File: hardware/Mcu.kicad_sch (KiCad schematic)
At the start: 9 parts, among them U10 STM32G484VEHx, Y1 X322516MLB4SI

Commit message: inductors 3d models fix, smaller relay (same series as the one from IMD), other + sync
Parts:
- added C70: 22uF, Capacitor_SMD:C_0805_2012Metric, symbol Device:C_Small
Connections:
- net +3.3V: now also C70.1
- net GND: now also C70.2
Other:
- moved on the sheet: C23, C24, C25, C28, C29

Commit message: all but the communications sections done
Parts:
- added R3: 0, Resistor_SMD:R_0603_1608Metric, symbol Device:R_Small
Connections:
- net +3.3V: now also R3.1; no longer C23.1, C24.1, C25.1, C28.1, C29.1, C70.1, U10.D5 (VDD), U10.D7 (VDD), U10.F5 (VDD), U10.F7 (VDD), U10.J5 (VDDA), U10.K5 (VREF+)
- new net +3.3VIO: C23.1, C24.1, C25.1, C28.1, C29.1, C70.1, R3.2, U10.D5 (VDD), U10.D7 (VDD), U10.F5 (VDD), U10.F7 (VDD), U10.J5 (VDDA), U10.K5 (VREF+)

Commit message: sync
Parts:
- added C36: 22uF, Capacitor_SMD:C_0805_2012Metric, symbol Device:C_Small
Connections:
- net +3.3VIO: now also C36.1
- net EN_12V: now also U10.F2 (PC0)
- net GND: now also C36.2
- net PG_12V: now also U10.F4 (PC1)
- net LTC_MISO renamed COM_MISO
- net LTC_MOSI renamed COM_MOSI
- net LTC_SCK renamed COM_SCK
- net SENS_IMD: no longer names the net of U10.J4 (PB2)
- net ~{LTC_CS} renamed ~{COM_CS}
- no-connect marks 38 -> 37
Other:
- note removed: "TIM5_CH1"
- moved on the sheet: C23, C24, C25, C28, C29, C70, R3

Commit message: sync
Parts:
- C23, C24, C25, C28, C29: Mouser Price/Stock (none) -> https://www.mouser.pl/ProductDetail/KEMET/C0603C104J3RACTU?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
- C36, C70: Mouser Price/Stock (none) -> https://www.mouser.pl/ProductDetail/Samsung-Electro-Mechani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
- U10: Mouser Part Number (none) -> 511-STM32G484VEH6; Mouser Price/Stock (none) -> https://www.mouser.pl/ProductDetail/STMicroelectronics/STM3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
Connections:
- net SPI_RDY: now reaches U10.F1 (PC2)
- net ~{FLT}: now reaches U10.G1 (PC3)
- no-connect marks 37 -> 35
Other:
- moved on the sheet: C36, C70, R3

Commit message: some routing done
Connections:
- net PG_12V: now also U10.G2 (PA1); no longer U10.F4 (PC1)
- net SIGNAL_AMS_ERROR: now also U10.J8 (PB10); no longer U10.H7 (PE15)
- net SIGNAL_LED_2: now also U10.H1 (PA2); no longer U10.H6 (PE9)
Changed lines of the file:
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@@
 	)
 	(no_connect
-		(at 111.76 46.99)
+		(at 71.12 90.17)
 	)
 	(no_connect
@@
 	)
 	(no_connect
-		(at 111.76 44.45)
+		(at 111.76 130.81)
 	)
 	(no_connect
@@
 	)
 	(no_connect
-		(at 111.76 110.49)
+		(at 71.12 105.41)
 	)
 	(no_connect
@@
 	(wire
 		(pts
-			(xy 71.12 90.17) (xy 68.58 90.17)
+			(xy 111.76 46.99) (xy 114.3 46.99)
 		)
 		(stroke
@@
 	(wire
 		(pts
-			(xy 71.12 105.41) (xy 68.58 105.41)
+			(xy 111.76 110.49) (xy 114.3 110.49)
 		)
 		(stroke
@@
 	(wire
 		(pts
-			(xy 114.3 130.81) (xy 111.76 130.81)
+			(xy 114.3 44.45) (xy 111.76 44.45)
 		)
 		(stroke
@@
 	(hierarchical_label "SIGNAL_AMS_ERROR"
 		(shape output)
-		(at 68.58 105.41 180)
-		(fields_autoplaced yes)
-		(effects
-			(font
-				(size 1.27 1.27)
-			)
-			(justify right)
+		(at 114.3 110.49 0)
+		(fields_autoplaced yes)
+		(effects
+			(font
+				(size 1.27 1.27)
+			)
+			(justify left)
 		)
 	)
@@
 	(hierarchical_label "SIGNAL_LED_2"
 		(shape input)
-		(at 68.58 90.17 180)
-		(fields_autoplaced yes)
-		(effects
-			(font
-				(size 1.27 1.27)
-			)
-			(justify right)
+		(at 114.3 46.99 0)
+		(fields_autoplaced yes)
+		(effects
+			(font
+				(size 1.27 1.27)
+			)
+			(justify left)
 		)
 	)
@@
 	(hierarchical_label "PG_12V"
 		(shape input)
-		(at 114.3 130.81 0)
-		(fields_autoplaced yes)
-		(effects
+		(at 114.3 44.45 0)
+		(fields_autoplaced yes)
+		(effects

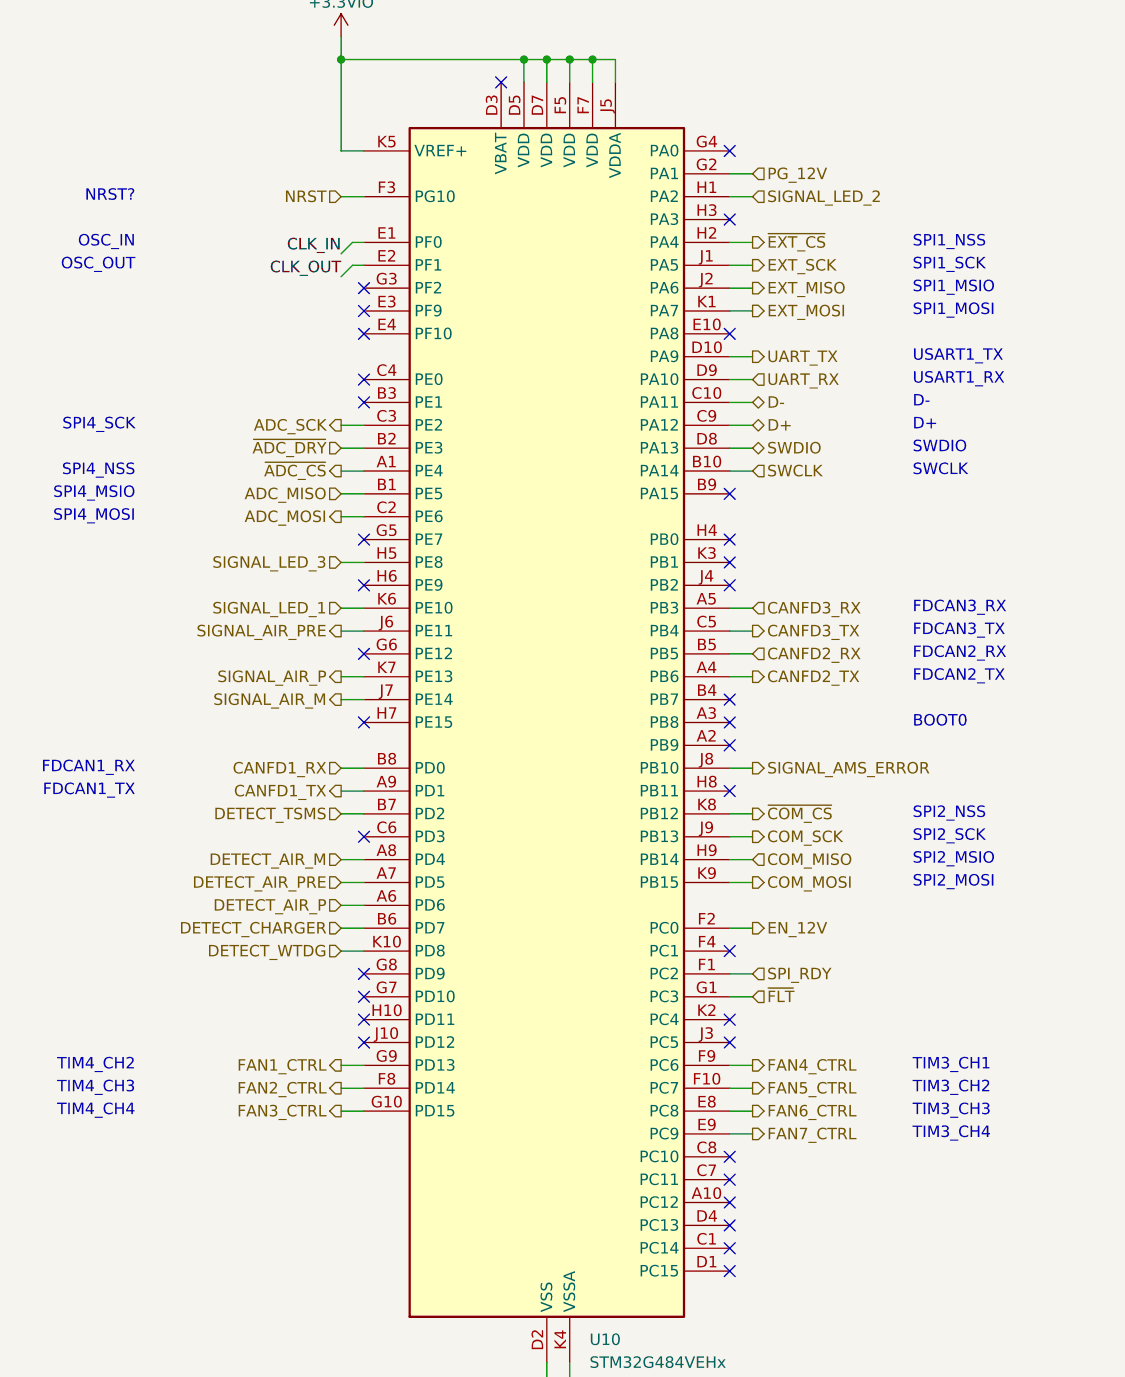
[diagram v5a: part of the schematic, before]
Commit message: routing done, drc checked
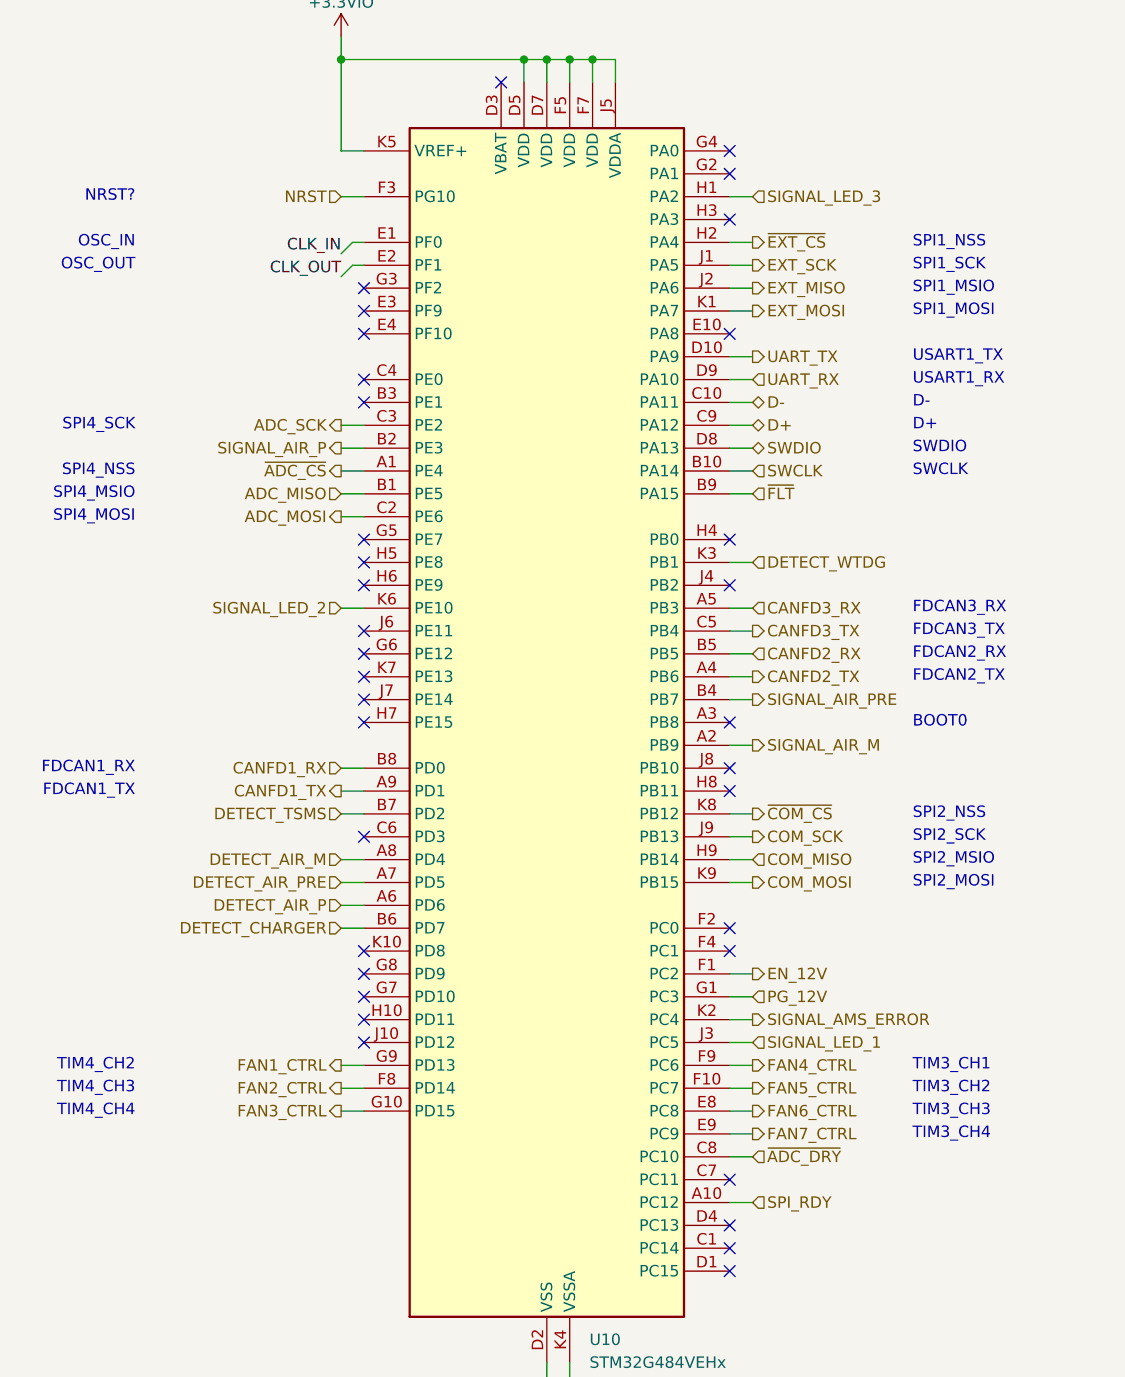
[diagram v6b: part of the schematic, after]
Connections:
- net DETECT_WTDG: now also U10.K3 (PB1); no longer U10.K10 (PD8)
- net EN_12V: now also U10.F1 (PC2); no longer U10.F2 (PC0)
- net PG_12V: now also U10.G1 (PC3); no longer U10.G2 (PA1)
- net SIGNAL_AIR_M: now also U10.A2 (PB9); no longer U10.J7 (PE14)
- net SIGNAL_AIR_P: now also U10.B2 (PE3); no longer U10.K7 (PE13)
- net SIGNAL_AIR_PRE: now also U10.B4 (PB7); no longer U10.J6 (PE11)
- net SIGNAL_AMS_ERROR: now also U10.K2 (PC4); no longer U10.J8 (PB10)
- net SIGNAL_LED_1: now also U10.J3 (PC5); no longer U10.K6 (PE10)
- net SIGNAL_LED_2: now also U10.K6 (PE10); no longer U10.H1 (PA2)
- net SIGNAL_LED_3: now also U10.H1 (PA2); no longer U10.H5 (PE8)
- net SPI_RDY: now also U10.A10 (PC12); no longer U10.F1 (PC2)
- net ~{ADC_DRY}: now also U10.C8 (PC10); no longer U10.B2 (PE3)
- net ~{FLT}: now also U10.B9 (PA15); no longer U10.G1 (PC3)

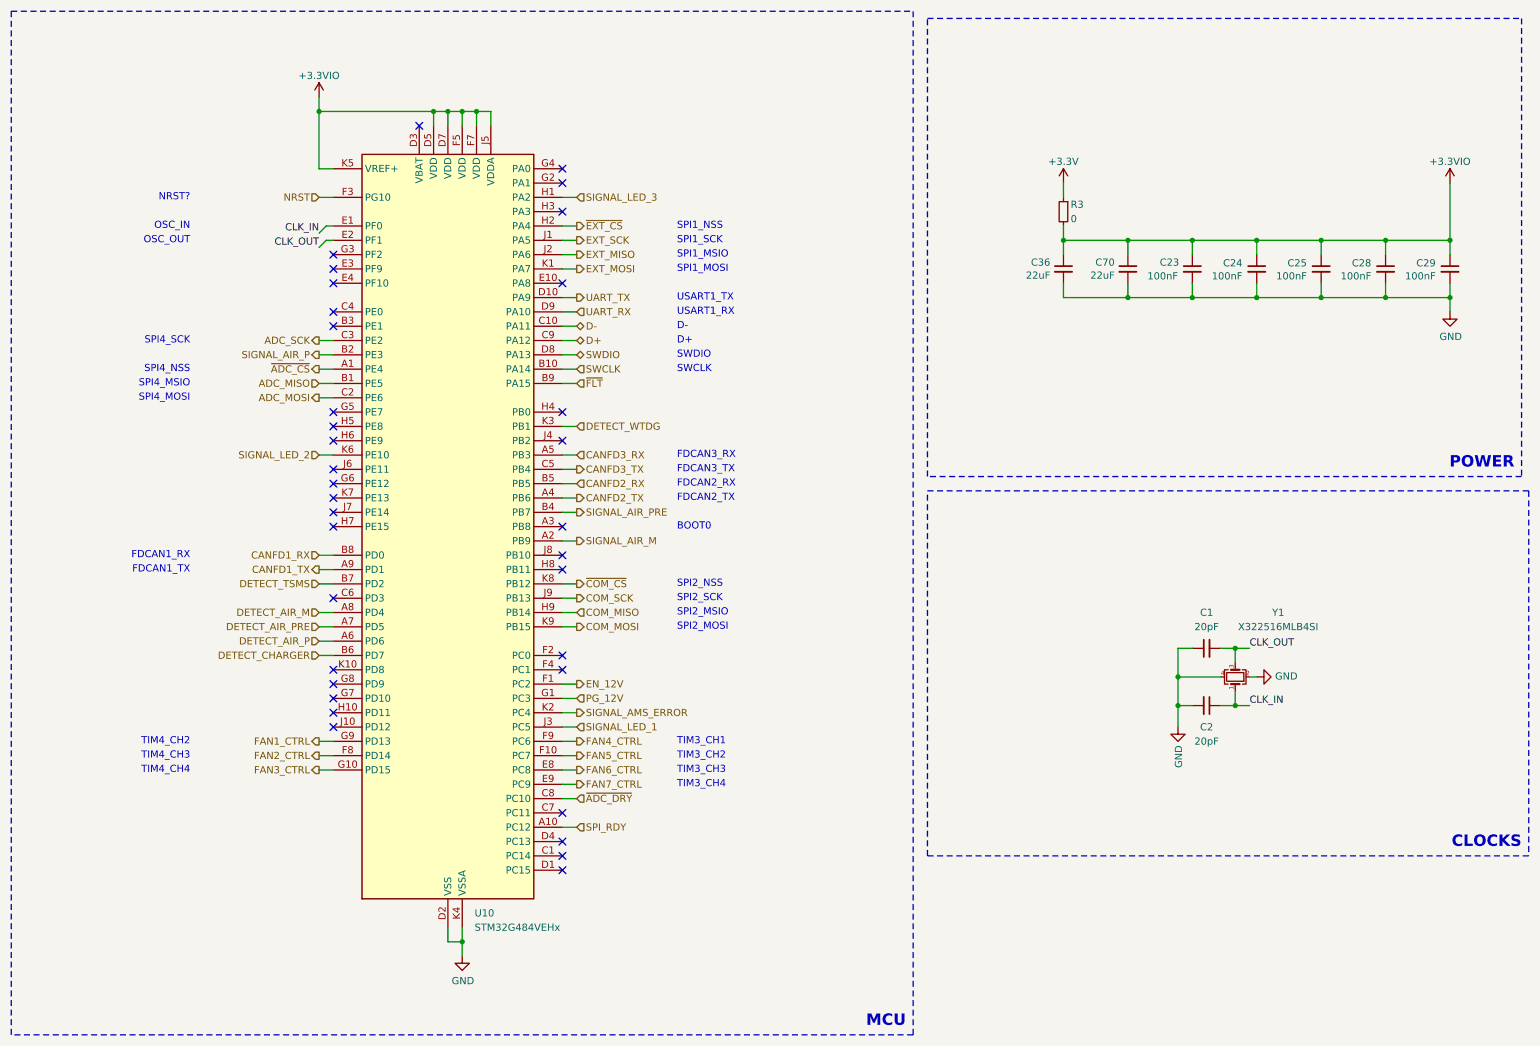
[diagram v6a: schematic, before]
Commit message: qfn mcu instead of bga sadge ;-;
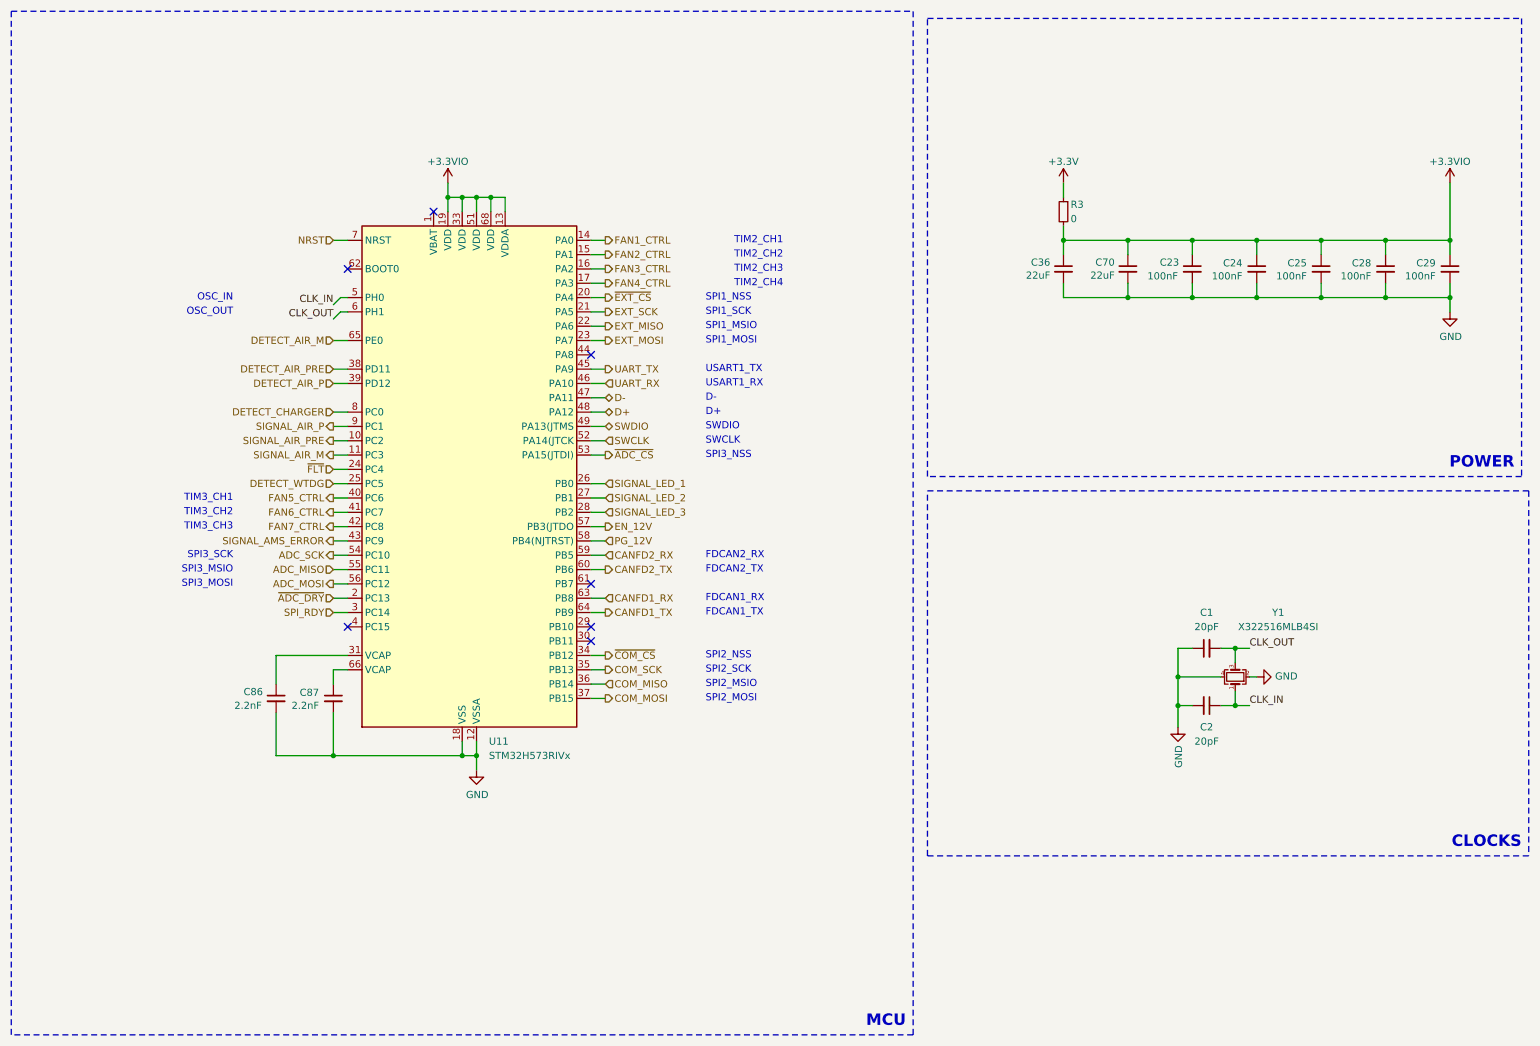
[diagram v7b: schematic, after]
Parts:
- removed U10: STM32G484VEHx, Package_BGA:TFBGA-100_8x8mm_Layout10x10_P0.8mm, symbol MCU_ST_STM32G4:STM32G484VEHx
- added C86, C87: 2.2nF, Capacitor_SMD:C_0402_1005Metric, symbol Device:C_Small
- added U11: STM32H573RIVx, Package_DFN_QFN:QFN-68-1EP_8x8mm_P0.4mm_EP5.2x5.2mm, symbol MCU_ST_STM32H5:STM32H573RIVx
- C23, C24, C25, C28, C29: footprint Capacitor_SMD:C_0402_1005Metric -> Capacitor_SMD:C_0603_1608Metric
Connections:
- net +3.3VIO: now also U11.13 (VDDA), U11.19 (VDD), U11.33 (VDD), U11.51 (VDD), U11.68 (VDD)
- net ADC_MISO: now also U11.55 (PC11)
- net ADC_MOSI: now also U11.56 (PC12)
- net ADC_SCK: now also U11.54 (PC10)
- net CANFD1_RX: now also U11.63 (PB8)
- net CANFD1_TX: now also U11.64 (PB9)
- net CANFD2_RX: now also U11.59 (PB5)
- net CANFD2_TX: now also U11.60 (PB6)
- net CLK_IN: now also U11.5 (PH0)
- net CLK_OUT: now also U11.6 (PH1)
- net COM_MISO: now also U11.36 (PB14)
- net COM_MOSI: now also U11.37 (PB15)
- net COM_SCK: now also U11.35 (PB13)
- net D+: now also U11.48 (PA12)
- net D-: now also U11.47 (PA11)
- net DETECT_AIR_M: now also U11.65 (PE0)
- net DETECT_AIR_P: now also U11.39 (PD12)
- net DETECT_AIR_PRE: now also U11.38 (PD11)
- net DETECT_CHARGER: now also U11.8 (PC0)
- net DETECT_WTDG: now also U11.25 (PC5)
- net EN_12V: now also U11.57 (PB3(JTDO)
- net EXT_MISO: now also U11.22 (PA6)
- net EXT_MOSI: now also U11.23 (PA7)
- net EXT_SCK: now also U11.21 (PA5)
- net FAN1_CTRL: now also U11.14 (PA0)
- net FAN2_CTRL: now also U11.15 (PA1)
- net FAN3_CTRL: now also U11.16 (PA2)
- net FAN4_CTRL: now also U11.17 (PA3)
- net FAN5_CTRL: now also U11.40 (PC6)
- net FAN6_CTRL: now also U11.41 (PC7)
- net FAN7_CTRL: now also U11.42 (PC8)
- net GND: now also C86.2, C87.2, U11.12 (VSSA), U11.18 (VSS), U11.32 (VSS), U11.50 (VSS), U11.67 (VSS), U11.69 (VSS)
- net NRST: now also U11.7 (NRST)
- net PG_12V: now also U11.58 (PB4(NJTRST))
- net SIGNAL_AIR_M: now also U11.11 (PC3)
- net SIGNAL_AIR_P: now also U11.9 (PC1)
- net SIGNAL_AIR_PRE: now also U11.10 (PC2)
- net SIGNAL_AMS_ERROR: now also U11.43 (PC9)
- net SIGNAL_LED_1: now also U11.26 (PB0)
- net SIGNAL_LED_2: now also U11.27 (PB1)
- net SIGNAL_LED_3: now also U11.28 (PB2)
- net SPI_RDY: now also U11.3 (PC14)
- net SWCLK: now also U11.52 (PA14(JTCK)
- net SWDIO: now also U11.49 (PA13(JTMS)
- net UART_RX: now also U11.46 (PA10)
- net UART_TX: now also U11.45 (PA9)
- net ~{ADC_CS}: now also U11.53 (PA15(JTDI))
- net ~{ADC_DRY}: now also U11.2 (PC13)
- net ~{COM_CS}: now also U11.34 (PB12)
- net ~{EXT_CS}: now also U11.20 (PA4)
- net ~{FLT}: now also U11.24 (PC4)
- new net: C87.1, U11.66 (VCAP)
- new net: C86.1, U11.31 (VCAP)
- no-connect marks 35 -> 7
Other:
- note added: "SPI3_MOSI"
- note added: "SPI3_MSIO"
- note added: "SPI3_NSS"
- note added: "SPI3_SCK"
- note added: "TIM2_CH1"
- note added: "TIM2_CH2"
- note added: "TIM2_CH3"
- note added: "TIM2_CH4"
- note removed: "BOOT0"
- note removed: "FDCAN3_RX"
- note removed: "FDCAN3_TX"
- note removed: "NRST?"
- note removed: "SPI4_MOSI"
- note removed: "SPI4_MSIO"
- note removed: "SPI4_NSS"
- note removed: "SPI4_SCK"
- note removed: "TIM3_CH4"
- note removed: "TIM4_CH2"
- note removed: "TIM4_CH3"
- note removed: "TIM4_CH4"
